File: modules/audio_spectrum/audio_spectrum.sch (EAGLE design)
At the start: 17 parts, among them J7 TC2030-JLINK-L, U1 SAM4LC8AA, X2 16MHz

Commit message: I think I finished the schematic
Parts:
- added C1, C25, C5, C6, C9: 0.1uF, passives:CAPACITOR0402_CAP
- added C10, C23, C8: 1nF, passives:CAPACITOR0402_CAP
- added C11, C19, C22: 1uF, passives:CAPACITOR0402_CAP
- added C12, C20: 100pF, passives:CAPACITOR0402_CAP
- added C18, C21: 4.7uF, passives:CAPACITOR0402_CAP
- added C2, C7: 33pF, passives:CAPACITOR0402_CAP
- added C24: 10uF, passives:CAPACITOR0402_CAP
- added C27: 3.3nF, passives:CAPACITOR0402_CAP
- added C28: 22uF, passives:CAPACITOR0402_CAP
- added J1: MODULE_GENERIC, signpost:MODULE_GENERIC
- added L1: 2.2uH, passives:INDUCTORIHL
- added P1, P2: 4k-200k, pots:POTTC33X
- added Q1, Q2: NX3008PBK, fets:NX3008PBK
- added R1, R2, R3, R4: 20k, passives:RESISTOR0402_RES
- added R10, R28: 100k, passives:RESISTOR0402_RES
- added R11, R8: 1.5k, passives:RESISTOR0402_RES
- added R14, R15: 10k, passives:RESISTOR0402_RES
- added R39: 240k, passives:RESISTOR0402_RES
- added R40: 750k, passives:RESISTOR0402_RES
- added R5, R6: 200k, passives:RESISTOR0402_RES
- added R7: 60k, passives:RESISTOR0402_RES
- added U$1: MP23AB02B, chips:MP23AB02B
- added U3: MSGEQ7, chips:MSGEQ7
- added U4: (no value), SparkFun-Connectors:AUDIO-JACKPTH
- added U5, U6: OPA344, SparkFun-AnalogIC:OPA344
- added U7: TLV62130, chips:TLV62130
- U2: value (none) -> MSGEQ7; device SparkFun-Connectors:AUDIO-JACKPTH -> chips:MSGEQ7
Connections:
- new net 3V3: C28.2, J1.VCCIO, J7.VCC, L1.2, Q1.S, Q2.S, R12.2, R20.2, R21.2, R28.2, R40.2, U7.VOS
- new net 3VSWOUT: L1.1, U7.SW
- new net 5V: C24.1, C25.1, J1.5V, U7.AVIN, U7.EN, U7.PVIN
- new net MOD_IN: J1.MOD_IN, U1.PA20
- new net MOD_OUT: J1.MOD_OUT, U1.PA19
- new net N$1: C1.1, U2.VSS
- new net N$10: C21.2, R14.2, R15.2
- new net N$11: C19.2, R1.2, R2.1, U6.+IN
- new net N$12: C12.2, P1.CW, R7.1, R8.2, U5.-IN
- new net N$13: C18.1, R8.1
- new net N$14: C20.2, P2.CW, R10.1, R11.2, U6.-IN
- new net N$15: C21.1, R11.1
- new net N$16: R15.1, U4.RIGHT
- new net N$17: R14.1, U4.LEFT
- new net N$18: C18.2, U$1.OUT
- new net N$2: C2.1, R5.2, U2.CLK
- new net N$3: C8.1, U2.IN
- new net N$34: C27.2, U7.SS/TR
- new net N$36: R28.1, U7.PG
- new net N$37: R39.2, R40.1, U7.FB
- new net N$4: C20.1, C8.2, P2.W, R10.2, U6.OUT
- new net N$5: C6.1, U3.VSS
- new net N$6: C7.1, R6.2, U3.CLK
- new net N$7: C10.1, U3.IN
- new net N$8: C10.2, C12.1, P1.W, R7.2, U5.OUT
- new net N$9: C11.2, R3.2, R4.1, U5.+IN
- new net PPS: J1.PPS, U1.PA18
- new net SCL: J1.SCL, U1.PA24
- new net SDA: J1.SDA, U1.PA23
- new net SPEC2_GATED: C5.1, Q1.D, R1.1, R5.1, U2.VDD, U6.V+
- new net SPEC2_OUT: U1.PA05, U2.OUT
- new net SPEC2_POWER: Q1.G, U1.PA15
- new net SPEC2_RESET: U1.PA17, U2.RESET
- new net SPEC2_STROBE: U1.PA16, U2.STROBE
- new net SPEC_GATED: C22.2, C23.2, C9.1, Q2.D, R3.1, R6.1, U$1.VDD, U3.VDD, U5.V+
- new net SPEC_OUT: U1.PA04, U3.OUT
- new net SPEC_POWER: Q2.G, U1.PA12
- new net SPEC_RESET: U1.PA14, U3.RESET
- new net SPEC_STROBE: U1.PA13, U3.STROBE
- new net USB+: J1.USB_D+, U1.PA26
- new net USB-: J1.USB_D-, U1.PA25
- net GND: now also C1.2, C11.1, C19.1, C2.2, C22.1, C23.1, C24.2, C25.2, C27.1, C28.1, C5.2, C6.2, C7.2, C9.2, J1.GND, R2.2, R39.1, R4.2, U$1.GND, U2.GND, U3.GND, U4.SLEEVE, U5.V-, U6.V-, U7.AGND, U7.DEF, U7.FSW, U7.PGND
- net VCC_CONTROLLER: no longer J7.VCC, R12.2, R20.2, R21.2
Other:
- note added: "DNP"
- note added: "Gain set to 40 (~32db) Potentiometer included as optional adjustment/debugging."
- note added: "Gain set to 67 (~36db) Potentiometer included as optional adjustment/debugging."

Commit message: did some routing
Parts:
- C1, C10, C11, C12, C18, C19, C2, C20, C21, C22, C23, C24, C25, C27, C28, C5, C6, C7, C8, C9: device passives:CAPACITOR0402_CAP -> passives:CAPACITOR0603_CAP
- R1, R10, R11, R14, R15, R2, R28, R3, R39, R4, R40, R5, R6, R7, R8: device passives:RESISTOR0402_RES -> passives:RESISTOR0603_RES

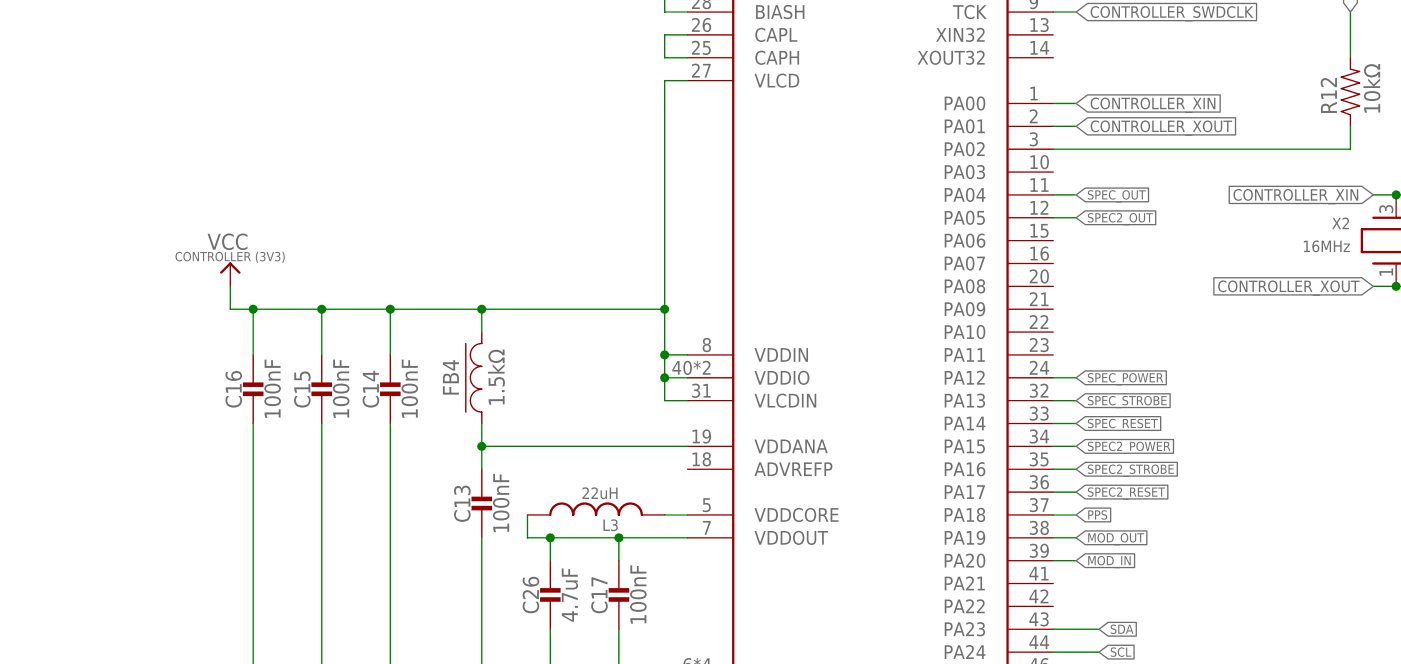
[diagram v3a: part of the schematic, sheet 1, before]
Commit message: no more airewires
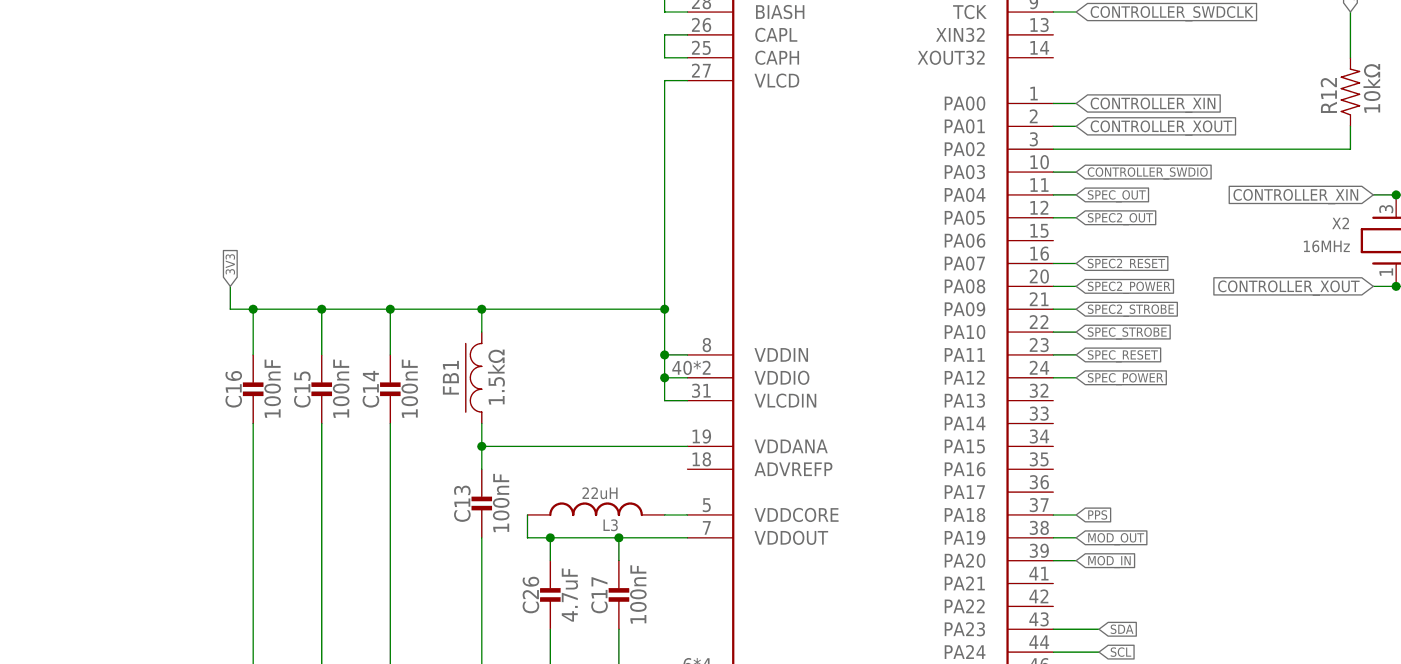
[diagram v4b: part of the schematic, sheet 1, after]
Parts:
- removed FB4: 1.5kΩ, passives:FERRITE_BEAD0402
- added FB1: 1.5kΩ, passives:FERRITE_BEAD0603
- C13, C14, C15, C16, C17, C26, C3, C4: device passives:CAPACITOR0402_CAP -> passives:CAPACITOR0603_CAP
- R12, R20, R21: device passives:RESISTOR0402_RES -> passives:RESISTOR0603_RES
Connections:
- removed net VCC_CONTROLLER: C14.1, C15.1, C16.1, FB4.P$2, U1.VDDIN, U1.VDDIO, U1.VLCD, U1.VLCDIN
- net 3V3: now also C14.1, C15.1, C16.1, FB1.P$2, U1.VDDIN, U1.VDDIO, U1.VLCD, U1.VLCDIN
- net CONTROLLER_SWDIO: now also U1.PA03
- net N$32: now also FB1.P$1; no longer FB4.P$1
- net SPEC2_POWER: now also U1.PA08; no longer U1.PA15
- net SPEC2_RESET: now also U1.PA07; no longer U1.PA17
- net SPEC2_STROBE: now also U1.PA09; no longer U1.PA16
- net SPEC_RESET: now also U1.PA11; no longer U1.PA14
- net SPEC_STROBE: now also U1.PA10; no longer U1.PA13

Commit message: added our version of the audio jack
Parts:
- U4: device SparkFun-Connectors:AUDIO-JACKPTH -> connector:AUDIO-JACKPTH
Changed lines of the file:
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@@
 <part name="FRAME2" library="lab11-frames" deviceset="LETTER_L_UMICH" device=""/>
 <part name="U2" library="chips" deviceset="MSGEQ7" device=""/>
-<part name="U4" library="SparkFun-Connectors" deviceset="AUDIO-JACK" device="PTH"/>
+<part name="U4" library="connector" deviceset="AUDIO-JACK" device="PTH"/>
 <part name="GND1" library="umich" deviceset="GND" device=""/>
 <part name="C1" library="passives" deviceset="CAPACITOR" device="0603_CAP" value="0.1uF"/>

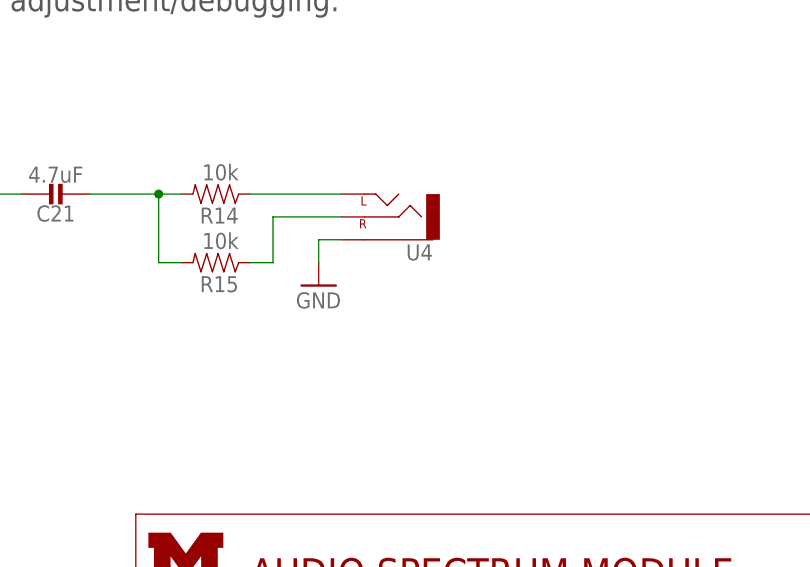
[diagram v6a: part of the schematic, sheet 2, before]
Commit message: fine I'll make 45 degree corners
I also added the vertical audio and
made the text bigger
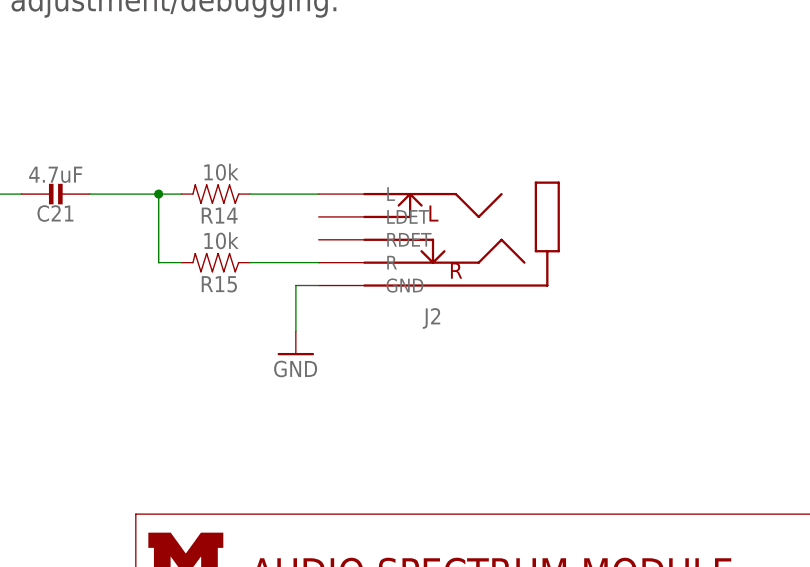
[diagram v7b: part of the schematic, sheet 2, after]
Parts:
- removed U4: (no value), connector:AUDIO-JACKPTH
- added J2: AUDIO-JACK-VERTICAL, connector:AUDIO-JACK-VERTICAL
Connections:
- net GND: now also J2.GND; no longer U4.SLEEVE
- net N$16: now also J2.R; no longer U4.RIGHT
- net N$17: now also J2.L; no longer U4.LEFT
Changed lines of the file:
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@@
 <part name="FRAME2" library="lab11-frames" deviceset="LETTER_L_UMICH" device=""/>
 <part name="U2" library="chips" deviceset="MSGEQ7" device=""/>
-<part name="U4" library="connector" deviceset="AUDIO-JACK" device="PTH"/>
 <part name="GND1" library="umich" deviceset="GND" device=""/>
 <part name="C1" library="passives" deviceset="CAPACITOR" device="0603_CAP" value="0.1uF"/>
@@
 <part name="L1" library="passives" deviceset="INDUCTOR" device="IHL" value="2.2uH"/>
 <part name="GND12" library="umich" deviceset="GND" device=""/>
+<part name="J2" library="connector" deviceset="AUDIO-JACK-VERTICAL" device=""/>
 </parts>
 <sheets>
@@
 <instance part="FRAME2" gate="G$2" x="147.32" y="0"/>
 <instance part="U2" gate="G$1" x="38.1" y="45.72"/>
-<instance part="U4" gate="G$1" x="175.26" y="53.34" rot="R180"/>
 <instance part="GND1" gate="1" x="30.48" y="10.16"/>
 <instance part="C1" gate="G$1" x="38.1" y="15.24" rot="R270"/>
@@
 <instance part="R14" gate="G$1" x="154.94" y="55.88" rot="R180"/>
 <instance part="R15" gate="G$1" x="154.94" y="48.26" rot="R180"/>
-<instance part="GND9" gate="1" x="167.64" y="45.72"/>
+<instance part="GND9" gate="1" x="165.1" y="38.1"/>
 <instance part="U$1" gate="G$1" x="177.8" y="129.54" rot="MR0"/>
 <instance part="GND10" gate="1" x="177.8" y="109.22"/>
@@
 <instance part="C23" gate="G$1" x="190.5" y="149.86" rot="R180"/>
 <instance part="GND11" gate="1" x="190.5" y="142.24"/>
+<instance part="J2" gate="G$1" x="172.72" y="55.88" rot="R180"/>
 </instances>
 <busses>
@@
 </segment>
 <segment>
-<pinref part="U4" gate="G$1" pin="SLEEVE"/>
 <pinref part="GND9" gate="1" pin="GND"/>
-<wire x1="170.18" y1="50.8" x2="167.64" y2="50.8" width="0.1524" layer="91"/>
-<wire x1="167.64" y1="50.8" x2="167.64" y2="48.26" width="0.1524" layer="91"/>
+<wire x1="165.1" y1="45.72" x2="165.1" y2="40.64" width="0.1524" layer="91"/>
+<pinref part="J2" gate="G$1" pin="GND"/>
+<wire x1="165.1" y1="45.72" x2="167.64" y2="45.72" width="0.1524" layer="91"/>
 </segment>
 <segment>
@@
 <segment>
 <pinref part="R15" gate="G$1" pin="1"/>
-<wire x1="160.02" y1="48.26" x2="162.56" y2="48.26" width="0.1524" layer="91"/>
-<wire x1="162.56" y1="48.26" x2="162.56" y2="53.34" width="0.1524" layer="91"/>
-<pinref part="U4" gate="G$1" pin="RIGHT"/>
-<wire x1="162.56" y1="53.34" x2="170.18" y2="53.34" width="0.1524" layer="91"/>
+<wire x1="160.02" y1="48.26" x2="167.64" y2="48.26" width="0.1524" layer="91"/>
+<pinref part="J2" gate="G$1" pin="R"/>
 </segment>
 </net>
@@
 <segment>
 <pinref part="R14" gate="G$1" pin="1"/>
-<pinref part="U4" gate="G$1" pin="LEFT"/>
-<wire x1="160.02" y1="55.88" x2="170.18" y2="55.88" width="0.1524" layer="91"/>
-</segment>
-</net>
+<wire x1="160.02" y1="55.88" x2="167.64" y2="55.88" width="0.1524" layer="91"/>
+<pinref part="J2" gate="G$1" pin="L"/>
+</segment>
+</net>
